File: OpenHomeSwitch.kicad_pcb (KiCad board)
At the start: 4 copper layers, 82.5 x 65.5 mm, 297 parts, among them J10 USB_C_Receptacle_USB2.0, J11 USB_C_Receptacle_USB2.0, J2 Conn_01x04, J3 Conn_01x04, J4 Micro_SD_Card_Det2, J5 Conn_01x04, J6 Extension I2C, J7 Conn_01x04, J8 Debug, J9 Extension UART, Q1 2N7002, Q10 MMBT3904, Q2 MMBT3904, Q3 MMBT3904, Q4 MMBT5401, Q5 AO3401A, Q6 MMBT5401, Q7 MMBT5401, Q8 AO3401A, Q9 MMBT5401, U1 RTL8367RB, U2 Allwinner_V3S, U3 TMI7003x, U4 TMI7003x, U5 W25Q128JVS, U6 SRV05-4, Y1 25MHz, Y2 24MHz, Y3 32.768kHz

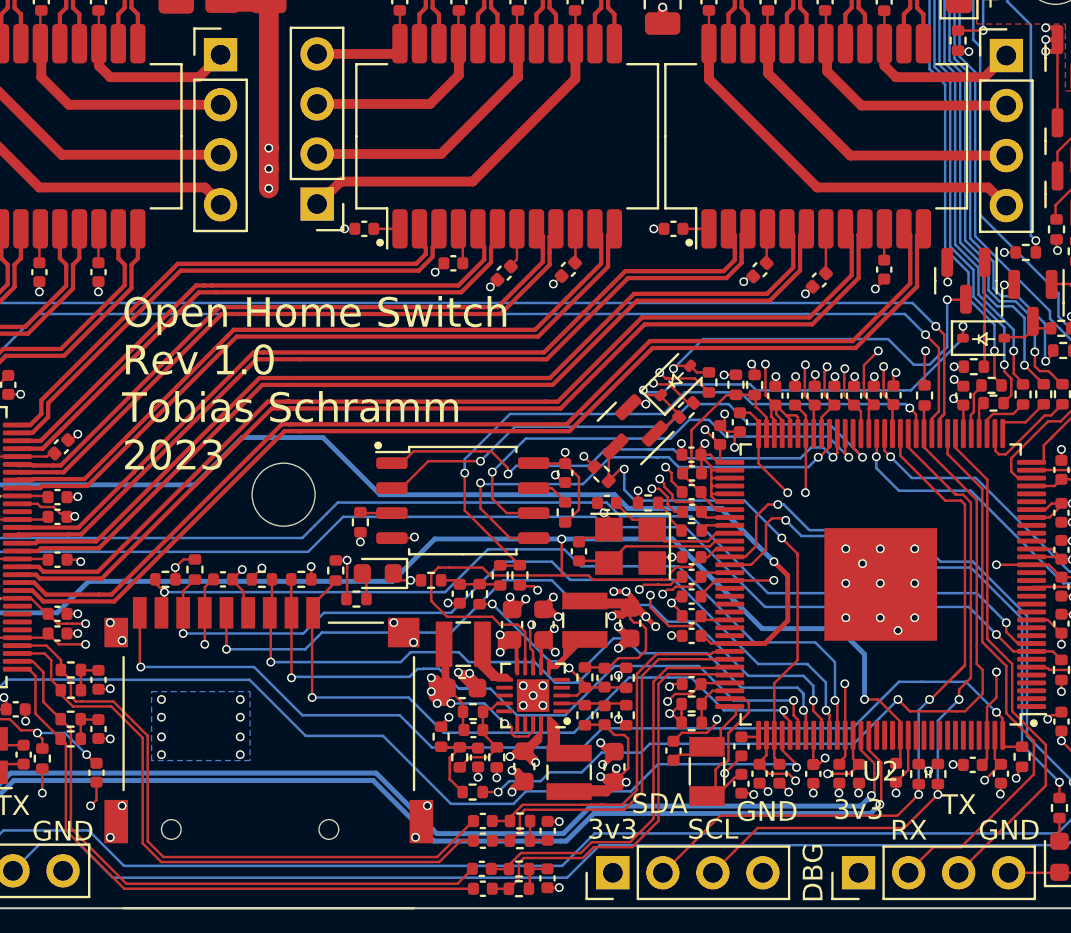
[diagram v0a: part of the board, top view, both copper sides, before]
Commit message: Add JLCJLCJLCJLC placeholder
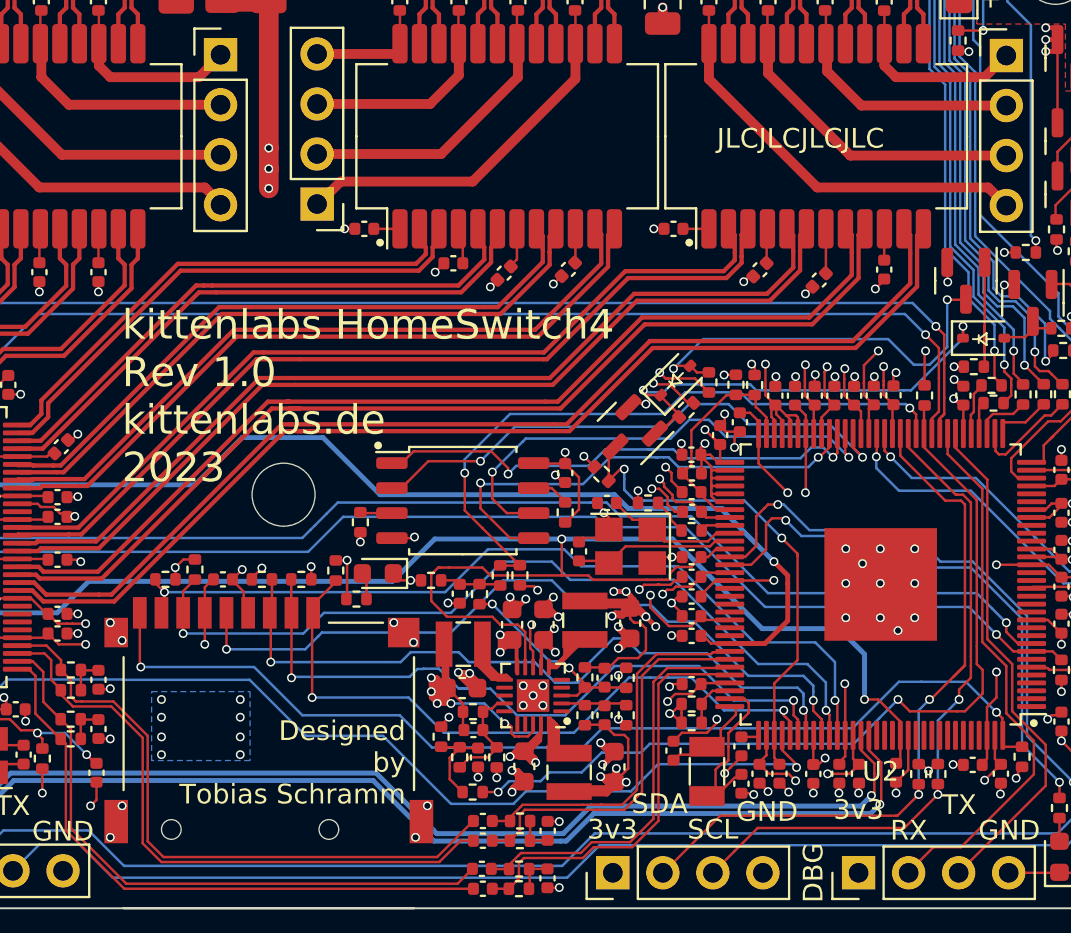
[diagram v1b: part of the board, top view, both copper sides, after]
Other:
- board text added: "Designed by Tobias Schramm"
- board text added: "JLCJLCJLCJLC"
- board text added: "kittenlabs HomeSwitch4 Rev 1.0 kittenlabs.de 2023"
- board text removed: "Open Home Switch Rev 1.0 Tobias Schramm 2023"
